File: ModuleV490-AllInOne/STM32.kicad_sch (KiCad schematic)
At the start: 45 parts, among them J10 TEMP2, J11 TEMP1, J12 TEMP2, J13 TEMP3, J2 BOOT_MODE, J3 UART_PROG, J4 ST_LINK, J8 TXRX, Q1 AO3401A, U13 EL3H7(B)(TA)-G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

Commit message: 14pF caps to 0402 parts (stock availability)
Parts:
- C30, C31: footprint Capacitor_SMD:C_0805_2012Metric -> Capacitor_SMD:C_0402_1005Metric; LCSCStockCode C519919 -> C458857; PartNumber CC0805JRNPO9BN140 -> 0402N140J500CT
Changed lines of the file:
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@@
       (effects (font (size 1.27 1.27)) (justify right))
     )
-    (property "Footprint" "Capacitor_SMD:C_0805_2012Metric" (at 26.035 86.36 0)
+    (property "Footprint" "Capacitor_SMD:C_0402_1005Metric" (at 26.035 86.36 0)
       (effects (font (size 1.27 1.27)) hide)
     )
@@
       (effects (font (size 1.27 1.27)) hide)
     )
-    (property "PartNumber" "CC0805JRNPO9BN140" (at 26.035 86.36 0)
-      (effects (font (size 1.27 1.27)) hide)
-    )
-    (property "LCSCStockCode" "C519919" (at 26.035 86.36 0)
+    (property "PartNumber" "0402N140J500CT" (at 26.035 86.36 0)
+      (effects (font (size 1.27 1.27)) hide)
+    )
+    (property "LCSCStockCode" "C458857" (at 26.035 86.36 0)
       (effects (font (size 1.27 1.27)) hide)
     )
@@
       (effects (font (size 1.27 1.27)) (justify right))
     )
-    (property "Footprint" "Capacitor_SMD:C_0805_2012Metric" (at 39.37 86.36 0)
+    (property "Footprint" "Capacitor_SMD:C_0402_1005Metric" (at 39.37 86.36 0)
       (effects (font (size 1.27 1.27)) hide)
     )
@@
       (effects (font (size 1.27 1.27)) hide)
     )
-    (property "PartNumber" "CC0805JRNPO9BN140" (at 39.37 86.36 0)
-      (effects (font (size 1.27 1.27)) hide)
-    )
-    (property "LCSCStockCode" "C519919" (at 39.37 86.36 0)
-      (effects (font (size 1.27 1.27)) hide)
-    )
+    (property "PartNumber" "0402N140J500CT" (at 39.37 86.36 0)
+      (effects (font (size 1.27 1.27)) hide)
+    )
+    (property "LCSCStockCode" "C458857" (at 39.37 86.36 0)
+      (effects (font (size 1.27 1.27)) hide)
+    )

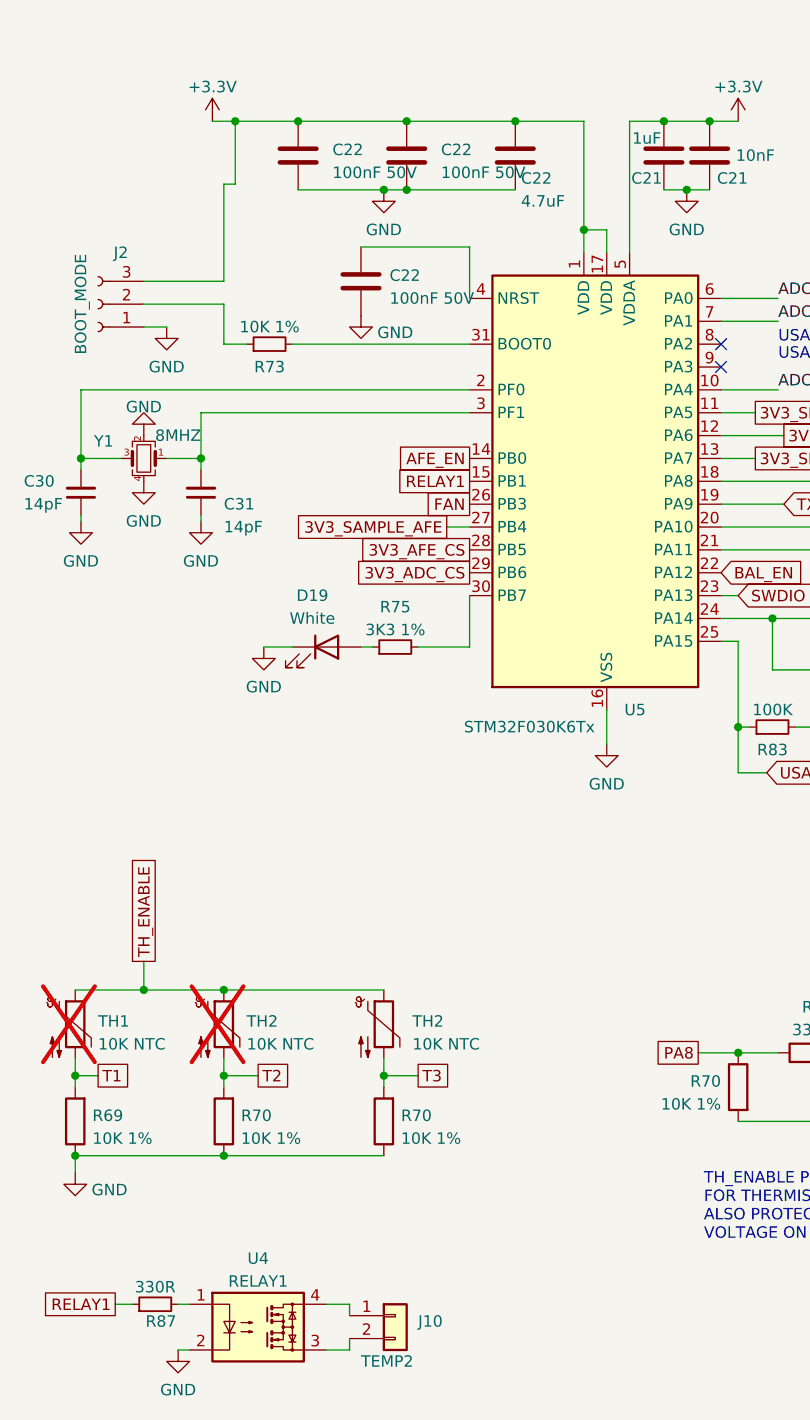
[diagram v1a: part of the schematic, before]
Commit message: Swap JST PH connectors to SMT - board size increase
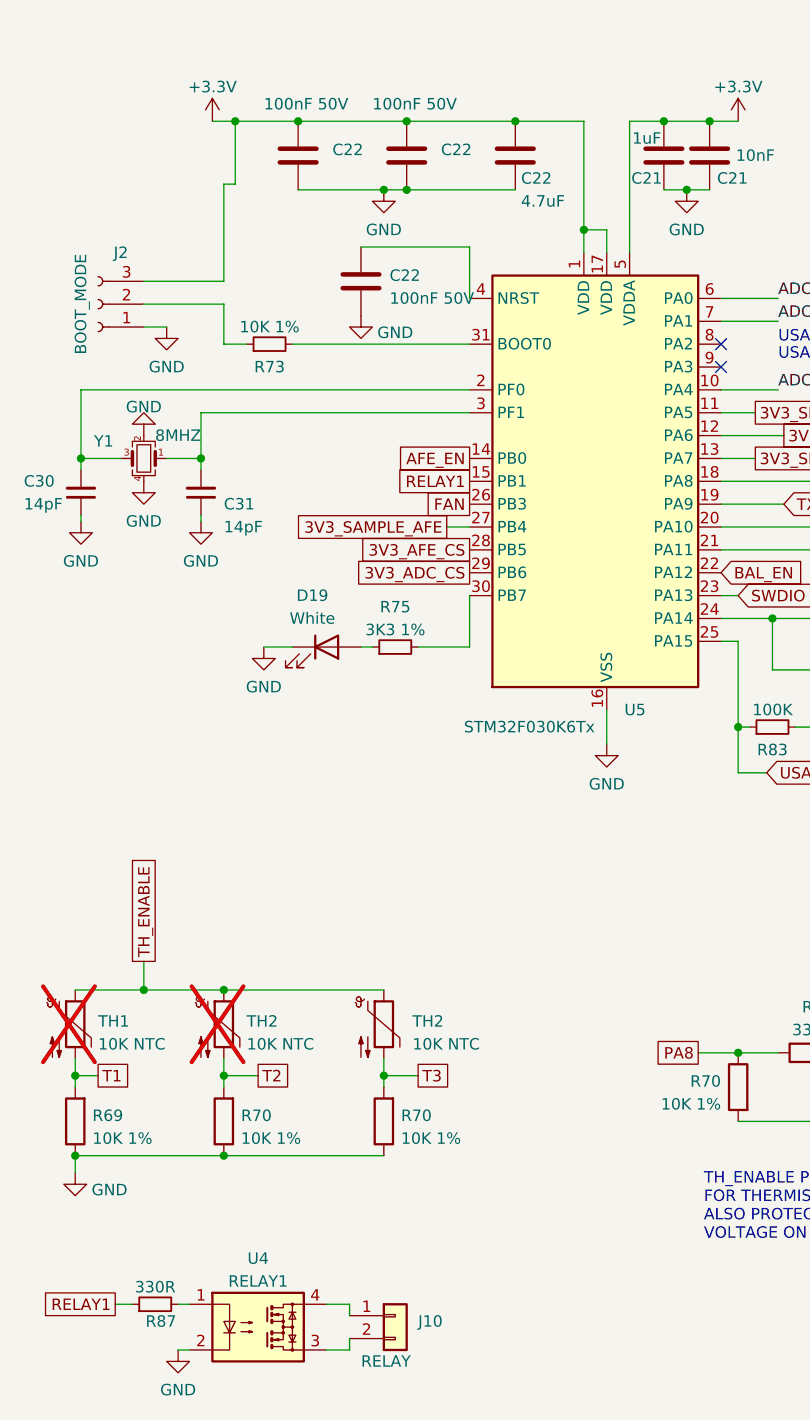
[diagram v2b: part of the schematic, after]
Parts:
- J10: value TEMP2 -> RELAY; footprint Connector_JST:JST_PH_S2B-PH-K_1x02_P2.00mm_Horizontal -> Connector_JST:JST_PH_S2B-PH-SM4-TB_1x02-1MP_P2.00mm_Horizontal; LCSCStockCode C265016 -> C295747; PartNumber S2B-PH-K(LF)(SN) -> S2B-PH-SM4-TB(LF)(SN)
- J11, J12, J13: footprint Connector_JST:JST_PH_S2B-PH-K_1x02_P2.00mm_Horizontal -> Connector_JST:JST_PH_S2B-PH-SM4-TB_1x02-1MP_P2.00mm_Horizontal; LCSCStockCode C265016 -> C295747; PartNumber S2B-PH-K(LF)(SN) -> S2B-PH-SM4-TB(LF)(SN)
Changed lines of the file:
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@@
   )
   (symbol (lib_id "Device:C") (at 50.165 48.895 180) (unit 1)
-    (in_bom yes) (on_board yes) (dnp no) (fields_autoplaced)
+    (in_bom yes) (on_board yes) (dnp no)
     (property "Reference" "C22" (at 53.975 48.26 0)
       (effects (font (size 1.27 1.27)) (justify right))
     )
-    (property "Value" "100nF 50V" (at 53.975 50.8 0)
+    (property "Value" "100nF 50V" (at 46.355 43.18 0)
       (effects (font (size 1.27 1.27)) (justify right))
     )
@@
   )
   (symbol (lib_id "Device:C") (at 62.23 48.895 180) (unit 1)
-    (in_bom yes) (on_board yes) (dnp no) (fields_autoplaced)
+    (in_bom yes) (on_board yes) (dnp no)
     (property "Reference" "C22" (at 66.04 48.26 0)
       (effects (font (size 1.27 1.27)) (justify right))
     )
-    (property "Value" "100nF 50V" (at 66.04 50.8 0)
+    (property "Value" "100nF 50V" (at 58.42 43.18 0)
       (effects (font (size 1.27 1.27)) (justify right))
     )
@@
       (effects (font (size 1.27 1.27)) (justify left))
     )
-    (property "Footprint" "Connector_JST:JST_PH_S2B-PH-K_1x02_P2.00mm_Horizontal" (at 201.93 141.605 0)
+    (property "Footprint" "Connector_JST:JST_PH_S2B-PH-SM4-TB_1x02-1MP_P2.00mm_Horizontal" (at 201.93 141.605 0)
       (effects (font (size 1.27 1.27)) hide)
     )
@@
       (effects (font (size 1.27 1.27)) hide)
     )
-    (property "PartNumber" "S2B-PH-K(LF)(SN)" (at 201.93 141.605 0)
-      (effects (font (size 1.27 1.27)) hide)
-    )
-    (property "LCSCStockCode" "C265016" (at 201.93 141.605 0)
+    (property "PartNumber" "S2B-PH-SM4-TB(LF)(SN)" (at 201.93 141.605 0)
+      (effects (font (size 1.27 1.27)) hide)
+    )
+    (property "LCSCStockCode" "C295747" (at 201.93 141.605 0)
       (effects (font (size 1.27 1.27)) hide)
     )
@@
       (effects (font (size 1.27 1.27)) (justify left))
     )
-    (property "Footprint" "Connector_JST:JST_PH_S2B-PH-K_1x02_P2.00mm_Horizontal" (at 226.06 142.24 0)
+    (property "Footprint" "Connector_JST:JST_PH_S2B-PH-SM4-TB_1x02-1MP_P2.00mm_Horizontal" (at 226.06 142.24 0)
       (effects (font (size 1.27 1.27)) hide)
     )
@@
       (effects (font (size 1.27 1.27)) hide)
     )
-    (property "PartNumber" "S2B-PH-K(LF)(SN)" (at 226.06 142.24 0)
-      (effects (font (size 1.27 1.27)) hide)
-    )
-    (property "LCSCStockCode" "C265016" (at 226.06 142.24 0)
+    (property "PartNumber" "S2B-PH-SM4-TB(LF)(SN)" (at 226.06 142.24 0)
+      (effects (font (size 1.27 1.27)) hide)
+    )
+    (property "LCSCStockCode" "C295747" (at 226.06 142.24 0)
       (effects (font (size 1.27 1.27)) hide)
     )
@@
       (effects (font (size 1.27 1.27)) (justify left))
     )
-    (property "Footprint" "Connector_JST:JST_PH_S2B-PH-K_1x02_P2.00mm_Horizontal" (at 249.555 143.51 0)
+    (property "Footprint" "Connector_JST:JST_PH_S2B-PH-SM4-TB_1x02-1MP_P2.00mm_Horizontal" (at 249.555 143.51 0)
       (effects (font (size 1.27 1.27)) hide)
     )
@@
       (effects (font (size 1.27 1.27)) hide)
     )
-    (property "PartNumber" "S2B-PH-K(LF)(SN)" (at 249.555 143.51 0)
-      (effects (font (size 1.27 1.27)) hide)
-    )
-    (property "LCSCStockCode" "C265016" (at 249.555 143.51 0)
+    (property "PartNumber" "S2B-PH-SM4-TB(LF)(SN)" (at 249.555 143.51 0)
+      (effects (font (size 1.27 1.27)) hide)
+    )
+    (property "LCSCStockCode" "C295747" (at 249.555 143.51 0)
       (effects (font (size 1.27 1.27)) hide)
     )
@@
       (effects (font (size 1.27 1.27)) (justify left))
     )
-    (property "Value" "TEMP2" (at 57.15 182.88 0)
-      (effects (font (size 1.27 1.27)) (justify left))
-    )
-    (property "Footprint" "Connector_JST:JST_PH_S2B-PH-K_1x02_P2.00mm_Horizontal" (at 60.96 177.8 0)
+    (property "Value" "RELAY" (at 57.15 182.88 0)
+      (effects (font (size 1.27 1.27)) (justify left))
+    )
+    (property "Footprint" "Connector_JST:JST_PH_S2B-PH-SM4-TB_1x02-1MP_P2.00mm_Horizontal" (at 60.96 177.8 0)
       (effects (font (size 1.27 1.27)) hide)
     )
@@
       (effects (font (size 1.27 1.27)) hide)
     )
-    (property "PartNumber" "S2B-PH-K(LF)(SN)" (at 60.96 177.8 0)
-      (effects (font (size 1.27 1.27)) hide)
-    )
-    (property "LCSCStockCode" "C265016" (at 60.96 177.8 0)
-      (effects (font (size 1.27 1.27)) hide)
-    )
+    (property "PartNumber" "S2B-PH-SM4-TB(LF)(SN)" (at 60.96 177.8 0)
+      (effects (font (size 1.27 1.27)) hide)
+    )
+    (property "LCSCStockCode" "C295747" (at 60.96 177.8 0)
+      (effects (font (size 1.27 1.27)) hide)
+    )
